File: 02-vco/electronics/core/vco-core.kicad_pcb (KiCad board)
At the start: 2 copper layers, 58 x 110 mm, 149 parts, among them J1 Conn_01x04, J2 Conn_02x05_Odd_Even, J3 Conn_02x05_Odd_Even, J4 Conn_01x02, J5 Conn_02x03_Odd_Even, J6 Conn_02x02_Counter_Clockwise, Q1 BC847BS, Q2 MMBT3906, Q3 J111, Q4 MMBFJ111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

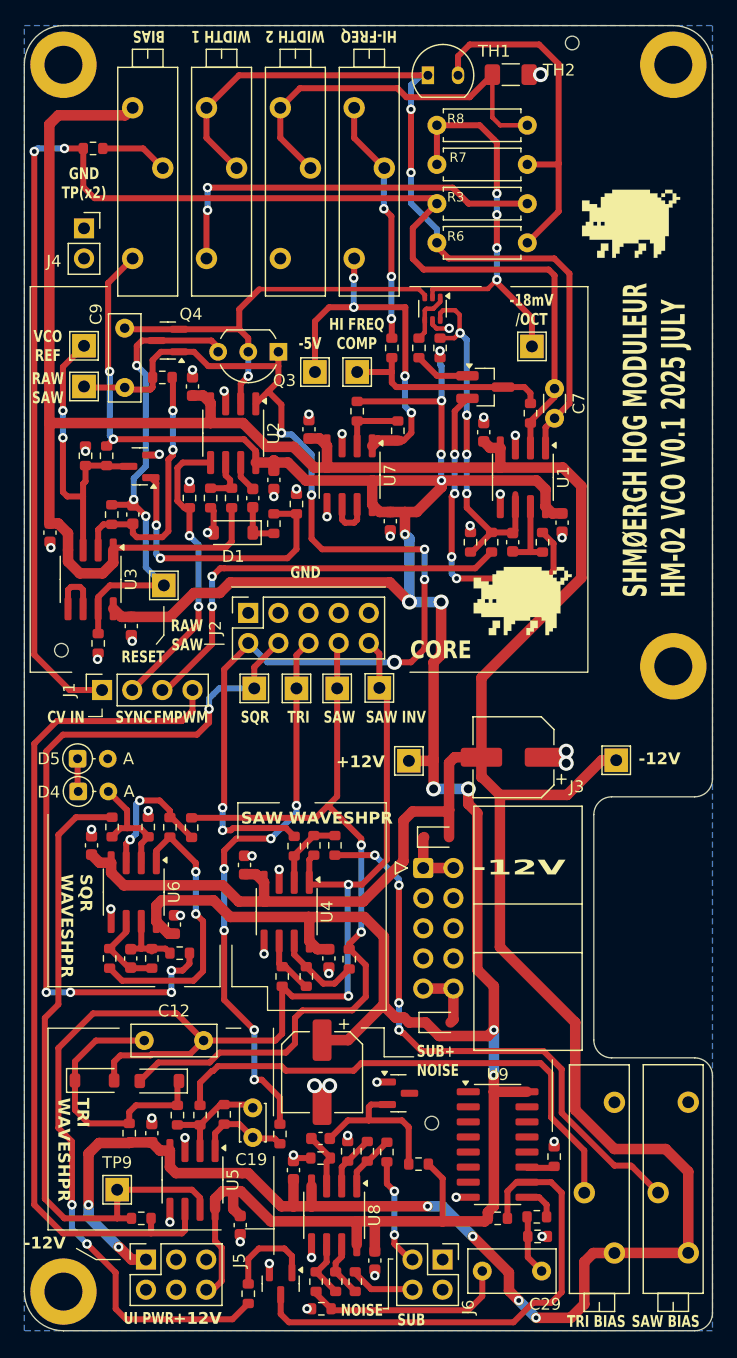
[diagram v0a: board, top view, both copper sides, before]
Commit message: Added VCO UI board
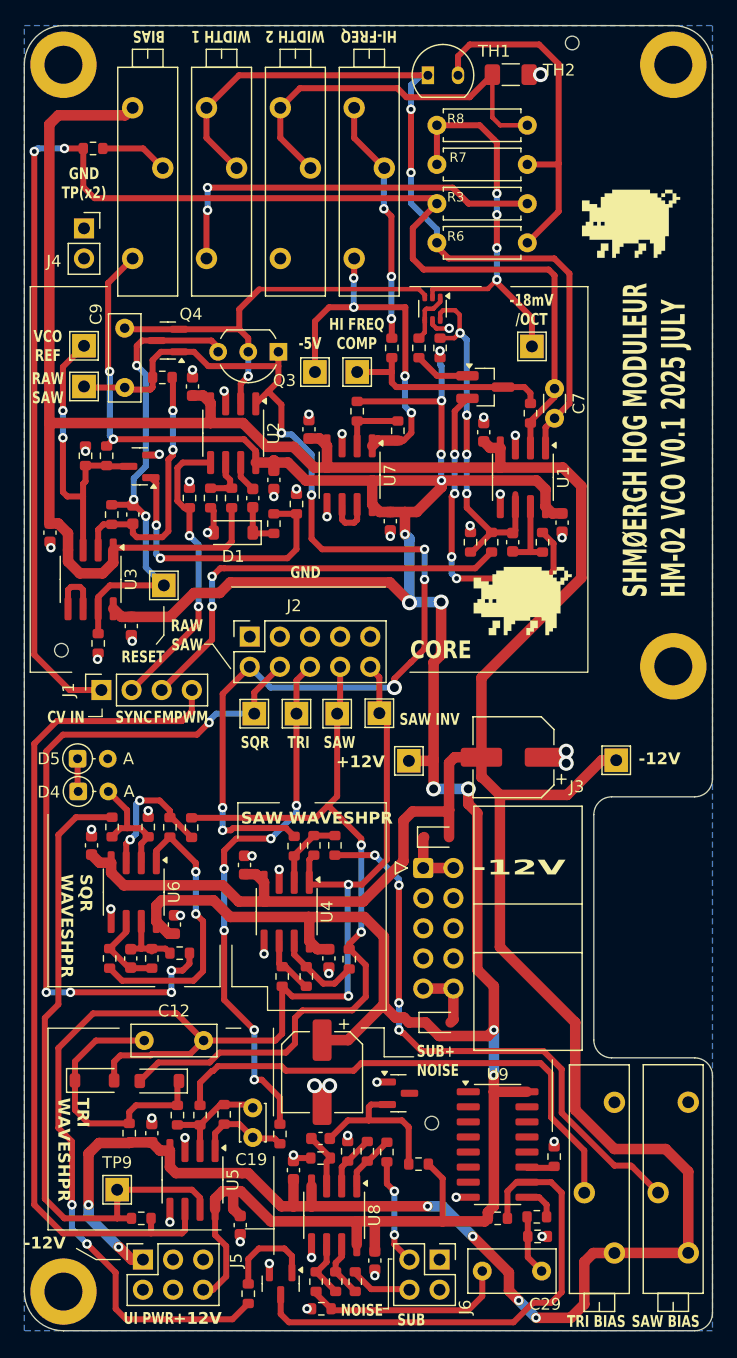
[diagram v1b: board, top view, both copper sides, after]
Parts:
- moved TP10 2.13 mm to (143.4, 102.0)
- moved TP7 2.13 mm to (150.4, 102.0)
- moved TP8 2.13 mm to (146.9, 102.0)
- moved TP6 2.13 mm to (153.9, 102.0)
- moved J2 2.00 mm to (143.0, 95.5)
- moved J6 0.26 mm to (159.0, 148.0)
- moved J5 0.25 mm to (134.0, 148.0)
- moved J1 0.06 mm to (130.5, 100.0)
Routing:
- net TRI: track 47.5 -> 45.4 mm
- net SQR: track 61.0 -> 59.0 mm
- net SAW: track 67.6 -> 65.7 mm
- net SAW_INV: track 115.4 -> 113.5 mm
- net +12V: track 282.7 -> 283.5 mm

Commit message: Updated sub circuit
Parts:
- removed R49, R51: 100k, Resistor_SMD:R_0603_1608Metric
- R48: value 47k -> 56k
- moved G*** 2.52 mm to (129.7, 132.9)
- moved C12 0.70 mm to (134.1, 128.8)
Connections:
- C29 pad 2: Net-(C29-Pad2) -> Net-(U8B-+)
- R44 pad 2: SAW_INV -> SAW
- R55 pad 1: Net-(R51-Pad1) -> Net-(U8B--)
- R56 pad 2: Net-(C29-Pad2) -> Net-(U8B-+)
- U8 pad 5: GND -> Net-(U8B-+)
- U8 pad 7: Net-(R51-Pad1) -> Net-(U8B--)
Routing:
- net SAW_INV: track 113.5 -> 63.7 mm, vias 4 -> 2
- net SAW: track 65.7 -> 101.4 mm, vias 2 -> 6
- net Net-(U8B-+): track 0.00 -> 21.5 mm
- net Net-(C29-Pad2): track 17.5 -> 0.00 mm
- net Net-(R51-Pad1): track 4.83 -> 0.00 mm
- net Net-(U8B--): track 5.03 -> 8.70 mm
- net GND: vias 48 -> 47

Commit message: Added default IO conn. to VCO core
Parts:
- removed the G*** at (166.0, 92.5)
- removed the G*** at (163.6, 99.0)
- added J8: Conn_01x06, Connector_PinSocket_2.54mm:PinSocket_1x06_P2.54mm_Vertical, F.Cu at (132.5, 151.0)
- J4: footprint Connector_PinSocket_2.54mm:PinSocket_1x02_P2.54mm_Vertical -> Connector_PinHeader_2.54mm:PinHeader_1x02_P2.54mm_Vertical
- moved J5 60.5 mm to (164.0, 95.5)
- moved R44 5.30 mm to (139.6, 146.7), turned to 180 degrees
- moved Q7 4.02 mm to (149.1, 151.9), turned to 0 degrees
- moved R56 3.25 mm to (148.9, 148.9)
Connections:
- J5 pad 1: -12V -> +12V
- J5 pad 6: +12V -> -12V
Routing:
- net -12V: track 339.4 -> 327.0 mm, vias 6 -> 4
- net SAW: track 101.4 -> 92.3 mm
- net Net-(Q7-C): track 42.6 -> 36.8 mm
- net +12V: track 283.5 -> 279.7 mm
- net Net-(Q7-B): track 7.81 -> 10.8 mm
- net Net-(U8B--): track 8.70 -> 6.61 mm
- net Net-(U8B-+): track 21.5 -> 20.3 mm
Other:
- board text added: "CV"
- board text added: "OUT"
- board text added: "SYN"

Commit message: Updated VCO core to use pin headers not sockets
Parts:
- J1: footprint Connector_PinSocket_2.54mm:PinSocket_1x04_P2.54mm_Vertical -> Connector_PinHeader_2.54mm:PinHeader_1x04_P2.54mm_Vertical
- J2: footprint Connector_PinSocket_2.54mm:PinSocket_2x05_P2.54mm_Vertical -> Connector_PinHeader_2.54mm:PinHeader_2x05_P2.54mm_Vertical
- J5: footprint Connector_PinSocket_2.54mm:PinSocket_2x03_P2.54mm_Vertical -> Connector_PinHeader_2.54mm:PinHeader_2x03_P2.54mm_Vertical
- J6: footprint Connector_PinSocket_2.54mm:PinSocket_2x02_P2.54mm_Vertical -> Connector_PinHeader_2.54mm:PinHeader_2x02_P2.54mm_Vertical
- J8: footprint Connector_PinSocket_2.54mm:PinSocket_1x06_P2.54mm_Vertical -> Connector_PinHeader_2.54mm:PinHeader_1x06_P2.54mm_Vertical
- moved J2 2.50 mm to (143.0, 98.0)
- moved J5 2.50 mm to (164.0, 98.0)
- moved J6 2.50 mm to (156.5, 148.0)
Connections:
- J2 pad 1: GND -> RAW_SAW
- J2 pad 10: SAW_INV -> GND
- J2 pad 2: RAW_SAW -> GND
- J2 pad 3: GND -> SQR
- J2 pad 4: SQR -> GND
- J2 pad 5: GND -> TRI
- J2 pad 6: TRI -> GND
- J2 pad 7: GND -> SAW
- J2 pad 8: SAW -> GND
- J2 pad 9: GND -> SAW_INV
- J5 pad 1: +12V -> GND
- J5 pad 2: GND -> +12V
- J5 pad 5: GND -> -12V
- J5 pad 6: -12V -> GND
- J6 pad 1: GND -> NOISE
- J6 pad 2: NOISE -> GND
- J6 pad 3: GND -> SUB
- J6 pad 4: SUB -> GND

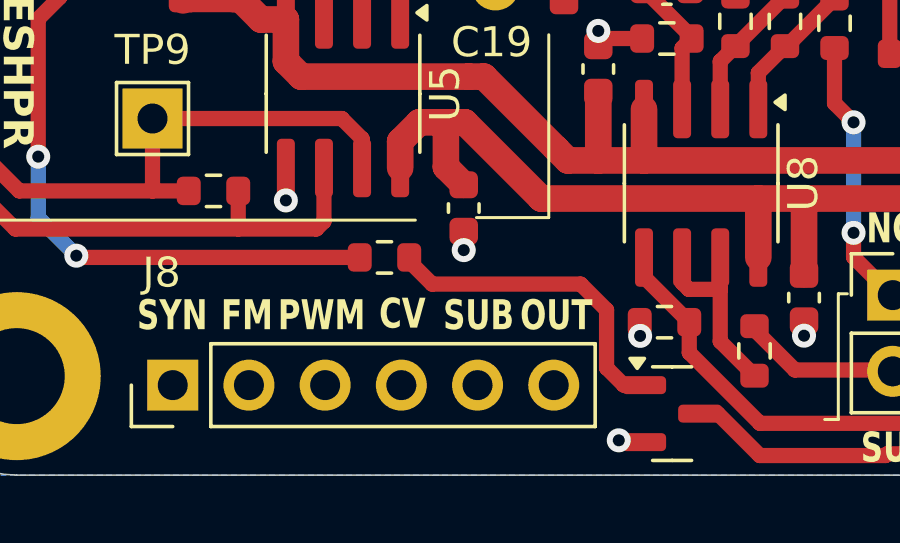
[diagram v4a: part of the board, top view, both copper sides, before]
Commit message: Added default IO to VCO UI board
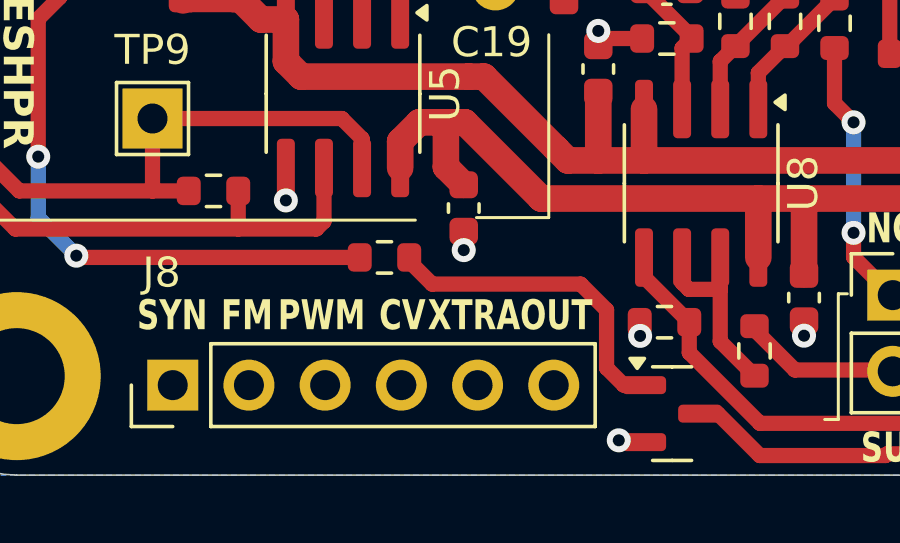
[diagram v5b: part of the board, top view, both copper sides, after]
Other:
- board text added: "XTRA"
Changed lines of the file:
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@@
 	)
 	(footprint "Connector_PinHeader_2.54mm:PinHeader_1x06_P2.54mm_Vertical"
+		(locked yes)
 		(layer "F.Cu")
 		(at 132.5 151 90)
@@
 		)
 	)
-	(gr_text "SUB"
-		(at 142.6944 149.2576 0)
+	(gr_text "XTRA"
+		(at 142.542 149.2576 0)
 		(layer "F.SilkS")
 		(effects
@@
 	)
 	(gr_text "CV"
-		(at 140.1544 149.2068 0)
+		(at 140.1544 149.2576 0)
 		(layer "F.SilkS")
 		(effects
@@
 	(gr_text "OUT"
 		(at 145.2852 149.2576 0)
-		(layer "F.SilkS")
+		(layer "F.SilkS" knockout)
 		(effects
 			(font

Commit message: Refined VCO core and UI
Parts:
- RV_SAW_BIAS1: value 10k -> 10k (prec)
- RV_TRI_BIAS1: value 100k -> 100k (prec)
